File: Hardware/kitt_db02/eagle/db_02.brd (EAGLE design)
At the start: 160 x 100 mm, 30 parts, among them T8.1 TPTP09SQ, T8.2 TPTP09SQ, U8 MCP23017ML, X8.1 CON_HEADER_1X08-SMD

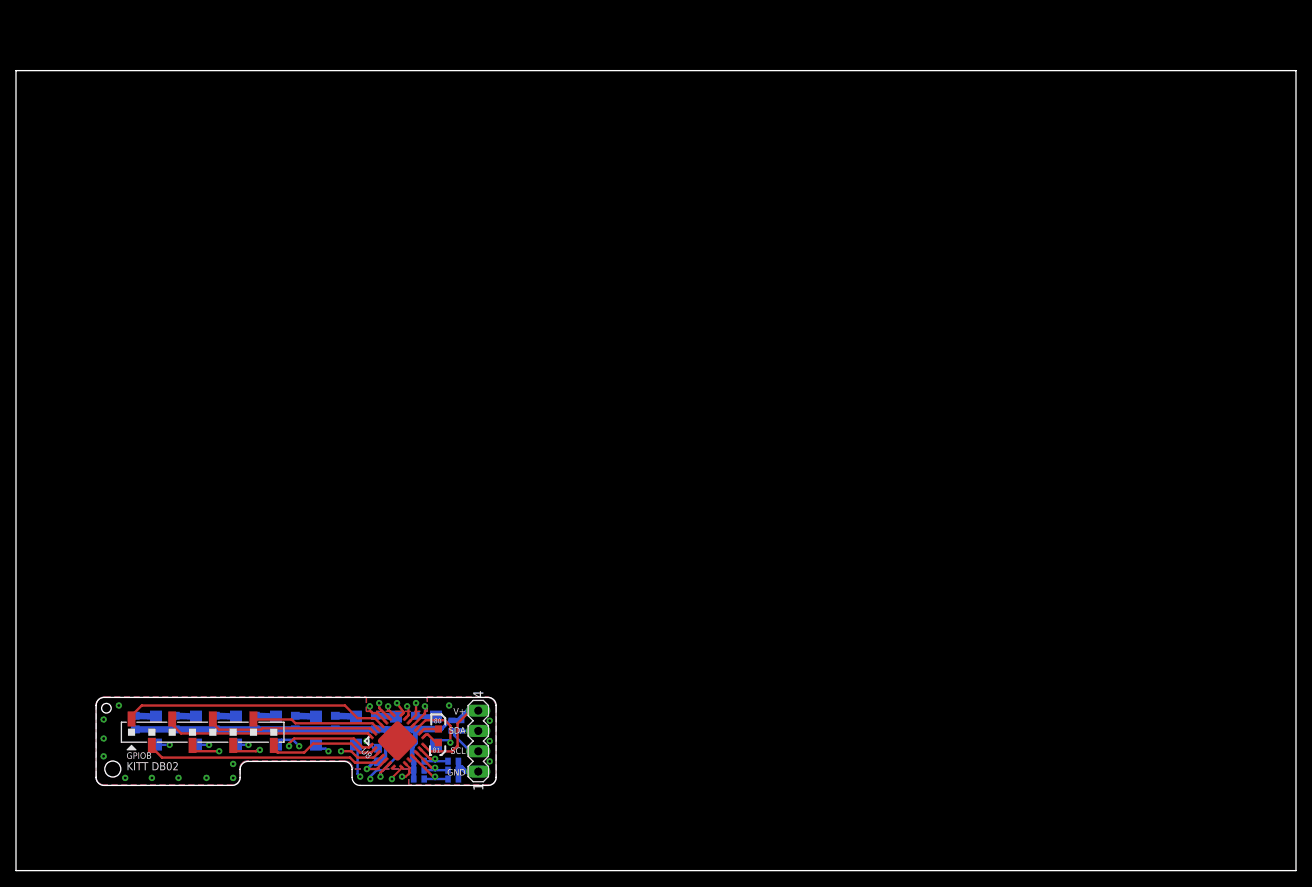
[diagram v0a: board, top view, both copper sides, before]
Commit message: minor touch ups on silkscreen layer
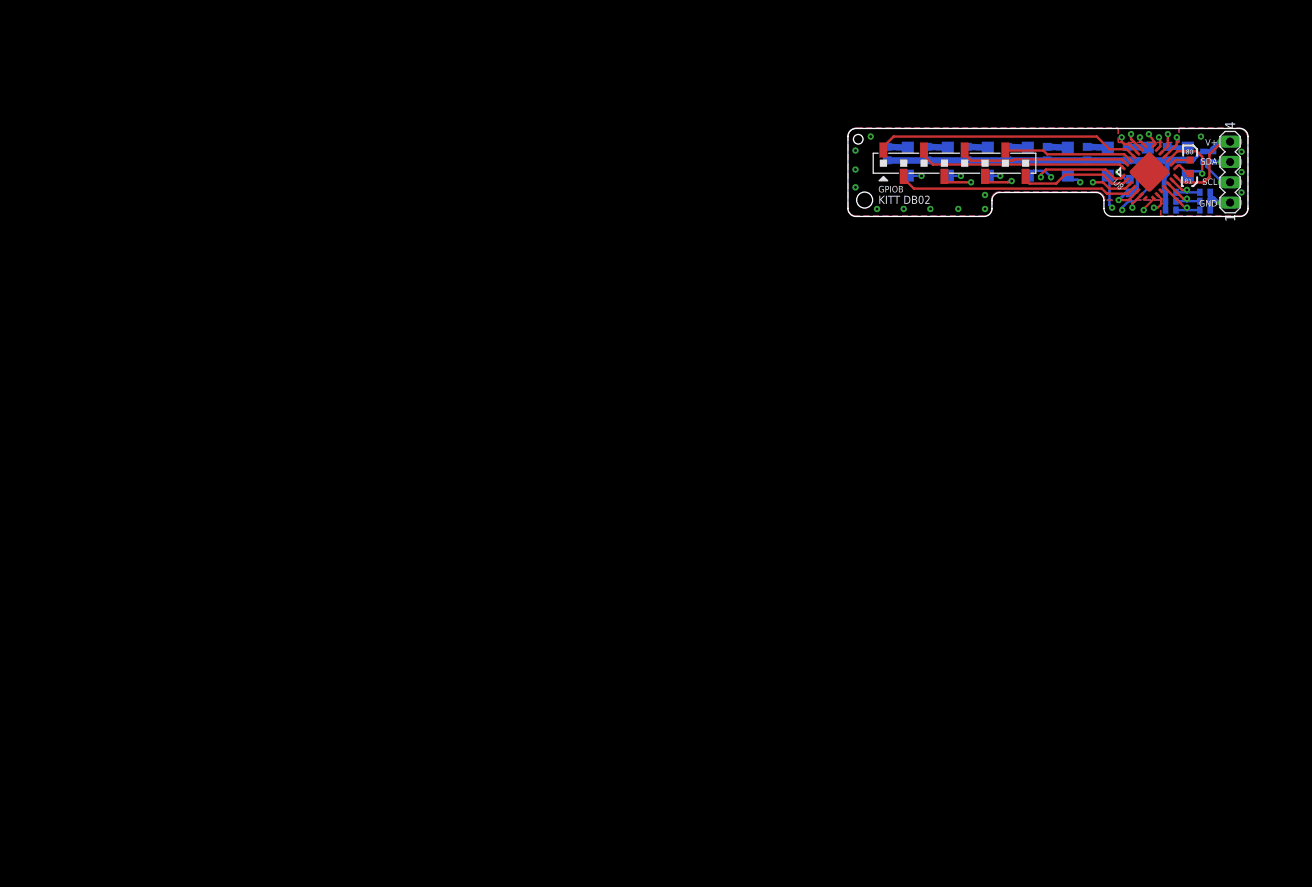
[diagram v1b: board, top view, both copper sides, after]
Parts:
- added U$1: (no value), frames:A4L-LOC
- moved R8.14 117.9 mm to (149.6, 89.2)
- moved C8.0 117.9 mm to (139.2, 85.6)
- moved D8.0 117.9 mm to (146.5, 88.6)
- moved D8.1 117.9 mm to (141.5, 88.6)
- moved D8.2 117.9 mm to (136.5, 88.6)
- moved D8.3 117.9 mm to (131.5, 88.6)
- moved D8.4 117.9 mm to (126.5, 88.6)
- moved D8.5 117.9 mm to (121.5, 88.6)
- moved D8.6 117.9 mm to (116.5, 88.6)
- moved D8.7 117.9 mm to (111.5, 88.6)
- moved R8.0 117.9 mm to (143.9, 89.6)
- moved R8.1 117.9 mm to (138.9, 89.6)
- moved R8.10 117.9 mm to (144.3, 84.8)
- moved R8.13 117.9 mm to (148.6, 84.8)
- moved R8.15 117.9 mm to (148.5, 89.2)
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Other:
- board size 160 x 100 mm -> 50 x 11 mm

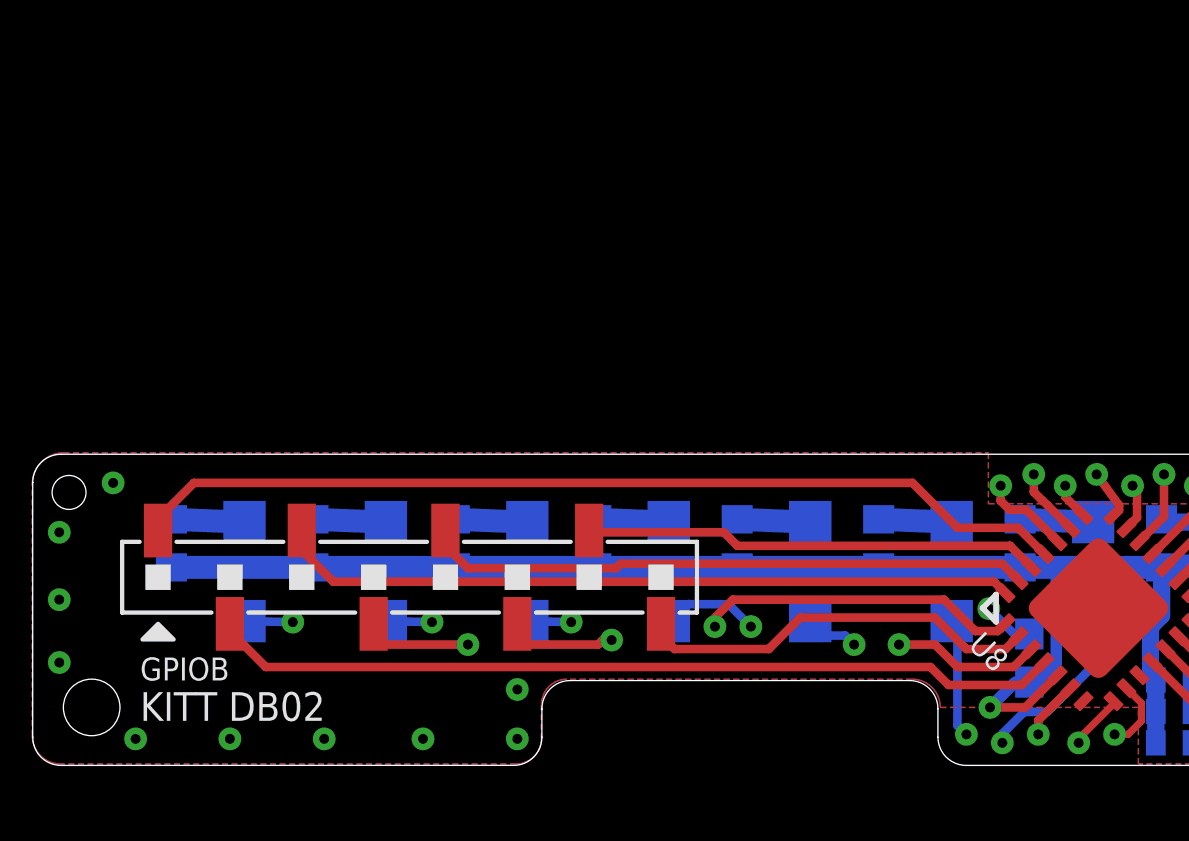
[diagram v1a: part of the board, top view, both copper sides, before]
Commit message: finished bill of materials for db02 -> layout needs a bit more work on the connector,    which now feature gnd and v+
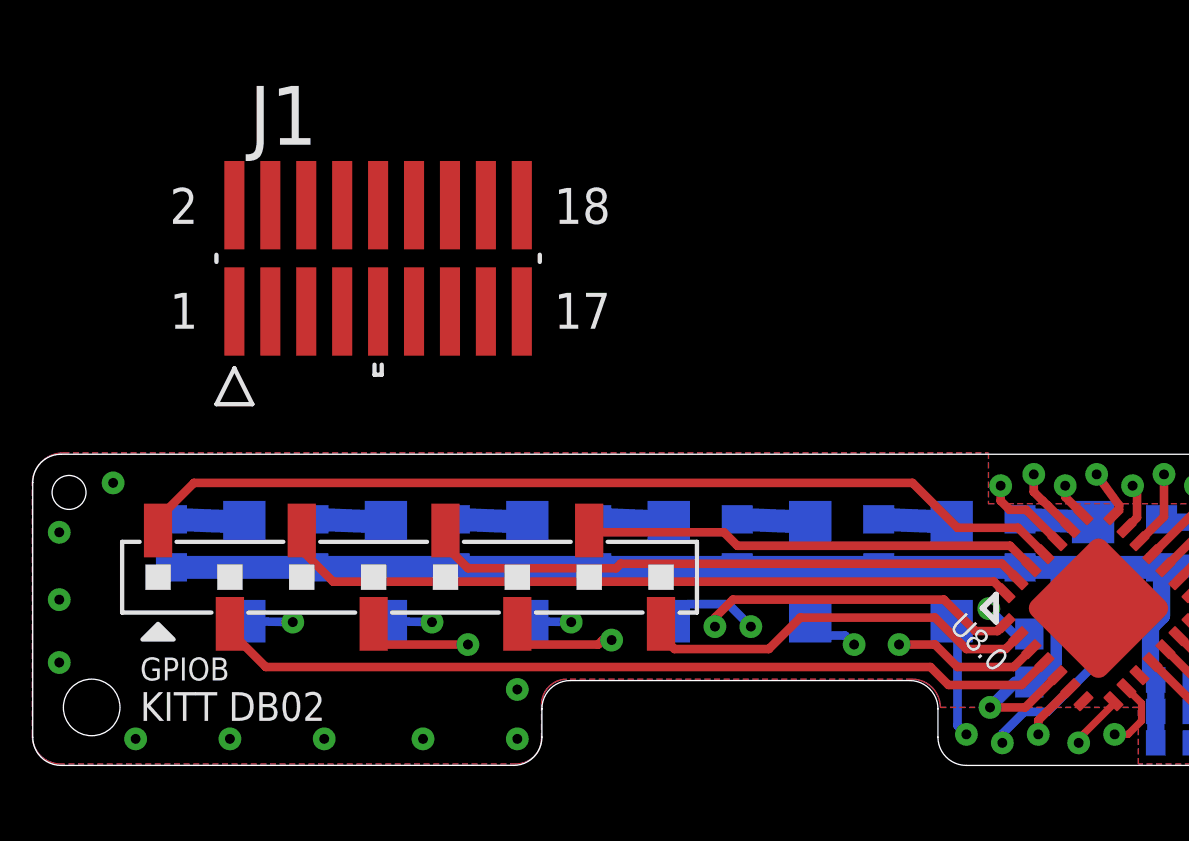
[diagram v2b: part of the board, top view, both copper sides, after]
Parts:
- added J1: FTS-109-01-L-DV, kitt.con:SAMTEC_FTS-109-01-L-DV
- renumbered U8 to U8.0
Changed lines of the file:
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@@
 <attribute name="VALUE" x="114.02" y="89.89" size="1.27" layer="28" rot="MR270"/>
 </element>
-<element name="U8" library="microchip" package="QFN28-ML_6X6MM" value="MCP23017ML" x="141.67" y="87.3275" smashed="yes" rot="R45">
+<element name="U8.0" library="microchip" package="QFN28-ML_6X6MM" value="MCP23017ML" x="141.67" y="87.3275" smashed="yes" rot="R45">
 <attribute name="MF" value="MICROCHIP" x="141.67" y="87.3275" size="1.778" layer="27" rot="R45" display="off"/>
 <attribute name="OC_FARNELL" value="unknown" x="141.67" y="87.3275" size="1.778" layer="27" rot="R45" display="off"/>
@@
 </element>
 <element name="U$1" library="frames" package="A4L-LOC" value="" x="0" y="0"/>
+<element name="J1" library="kitt.con" package="SAMTEC_FTS-109-01-L-DV" value="FTS-109-01-L-DV" x="116.205" y="99.695">
+<attribute name="MF" value="Samtec" x="116.205" y="99.695" size="1.778" layer="27" display="off"/>
+<attribute name="PRICE" value="2.67 USD" x="116.205" y="99.695" size="1.778" layer="27" display="off"/>
+<attribute name="PACKAGE" value="None" x="116.205" y="99.695" size="1.778" layer="27" display="off"/>
+<attribute name="MP" value="FTS-109-01-L-DV" x="116.205" y="99.695" size="1.778" layer="27" display="off"/>
+<attribute name="AVAILABILITY" value="Warning" x="116.205" y="99.695" size="1.778" layer="27" display="off"/>
+<attribute name="DESCRIPTION" value="Conn Unshrouded Header HDR 18 POS 1.27mm Solder ST SMD Tube" x="116.205" y="99.695" size="1.778" layer="27" display="off"/>
+</element>
 </elements>
 <signals>
 <signal name="N$1">
-<contactref element="U8" pad="17"/>
+<contactref element="U8.0" pad="17"/>
 <contactref element="D8.0" pad="C"/>
 <wire x1="148.28" y1="87.12" x2="148.03" y2="87.42" width="0.3048" layer="16"/>
@@
 </signal>
 <signal name="N$2">
-<contactref element="U8" pad="18"/>
+<contactref element="U8.0" pad="18"/>
 <contactref element="D8.1" pad="C"/>
 <wire x1="143.5791875" y1="89.2366875" x2="145.0975" y2="90.755" width="0.3048" layer="1"/>
@@
 </signal>
 <signal name="N$3">
-<contactref element="U8" pad="19"/>
+<contactref element="U8.0" pad="19"/>
 <contactref element="D8.2" pad="C"/>
 <wire x1="143.11956875" y1="89.69630625" x2="143.98625" y2="90.5629875" width="0.3048" layer="1"/>
@@
 </signal>
 <signal name="N$4">
-<contactref element="U8" pad="20"/>
+<contactref element="U8.0" pad="20"/>
 <contactref element="D8.3" pad="C"/>
 <wire x1="142.659946875" y1="90.155925" x2="143.03375" y2="90.529728125" width="0.3048" layer="1"/>
@@
 </signal>
 <signal name="N$5">
-<contactref element="U8" pad="21"/>
+<contactref element="U8.0" pad="21"/>
 <contactref element="D8.4" pad="C"/>
 <wire x1="142.200328125" y1="90.61554375" x2="142.20929375" y2="90.61554375" width="0.3048" layer="1"/>
@@
 </signal>
 <signal name="N$6">
-<contactref element="U8" pad="22"/>
+<contactref element="U8.0" pad="22"/>
 <contactref element="D8.5" pad="C"/>
 <wire x1="141.13966875" y1="90.61554375" x2="140.49375" y2="91.2614625" width="0.3048" layer="1"/>
@@
 </signal>
 <signal name="N$7">
-<contactref element="U8" pad="23"/>
+<contactref element="U8.0" pad="23"/>
 <contactref element="D8.6" pad="C"/>
 <wire x1="140.68005" y1="90.155925" x2="139.872225" y2="90.96375" width="0.3048" layer="1"/>
@@
 </signal>
 <signal name="N$8">
-<contactref element="U8" pad="24"/>
+<contactref element="U8.0" pad="24"/>
 <contactref element="D8.7" pad="C"/>
 <wire x1="140.220428125" y1="89.69630625" x2="139.111734375" y2="90.805" width="0.3048" layer="1"/>
@@
 <wire x1="143.9" y1="88.77" x2="140.17625" y2="88.77" width="0.8128" layer="16"/>
 <contactref element="X8.0" pad="4"/>
-<contactref element="U8" pad="5"/>
+<contactref element="U8.0" pad="5"/>
 <contactref element="R8.14" pad="2"/>
 <contactref element="R8.15" pad="2"/>
@@
 <wire x1="143.51" y1="86.6775" x2="143.9" y2="87.0675" width="0.6096" layer="16"/>
 <wire x1="143.9" y1="87.0675" x2="143.9" y2="88.77" width="0.6096" layer="16"/>
-<contactref element="U8" pad="14"/>
+<contactref element="U8.0" pad="14"/>
 <contactref element="C8.0" pad="1"/>
 <via x="137.83625" y="83.82" extent="1-16" drill="0.35"/>
@@
 <signal name="GND">
 <contactref element="X8.0" pad="1"/>
-<contactref element="U8" pad="6"/>
+<contactref element="U8.0" pad="6"/>
 <wire x1="139.54125" y1="82.8675" x2="139.54125" y2="83.360271875" width="0.3048" layer="1"/>
 <wire x1="139.54125" y1="83.360271875" x2="140.68005" y2="84.499071875" width="0.3048" layer="1"/>
@@
 <contactref element="X8.0" pad="3"/>
 <contactref element="R8.14" pad="1"/>
-<contactref element="U8" pad="8"/>
+<contactref element="U8.0" pad="8"/>
 <wire x1="142.200328125" y1="84.039453125" x2="142.24" y2="83.99978125" width="0.254" layer="1"/>
 <via x="140.97" y="82.5675" extent="1-16" drill="0.35"/>
@@
 <contactref element="X8.0" pad="2"/>
 <contactref element="R8.15" pad="1"/>
-<contactref element="U8" pad="9"/>
+<contactref element="U8.0" pad="9"/>
 <wire x1="142.659946875" y1="84.499071875" x2="143.1925" y2="83.96651875" width="0.254" layer="1"/>
 <wire x1="143.1925" y1="83.96651875" x2="143.1925" y2="83.34375" width="0.254" layer="1"/>
@@
 <contactref element="R8.8" pad="1"/>
 <contactref element="R8.11" pad="2"/>
-<contactref element="U8" pad="11"/>
+<contactref element="U8.0" pad="11"/>
 <wire x1="143.5791875" y1="85.418309375" x2="146.129996875" y2="82.8675" width="0.3048" layer="1"/>
 <wire x1="146.129996875" y1="82.8675" x2="146.3675" y2="82.8675" width="0.3048" layer="1"/>
@@
 <contactref element="R8.9" pad="1"/>
 <contactref element="R8.12" pad="2"/>
-<contactref element="U8" pad="12"/>
+<contactref element="U8.0" pad="12"/>
 <wire x1="144.03880625" y1="85.877928125" x2="145.937984375" y2="83.97875" width="0.3048" layer="1"/>
 <wire x1="145.937984375" y1="83.97875" x2="146.3675" y2="83.97875" width="0.3048" layer="1"/>
@@
 <contactref element="R8.10" pad="1"/>
 <contactref element="R8.13" pad="2"/>
-<contactref element="U8" pad="13"/>
+<contactref element="U8.0" pad="13"/>
 <wire x1="144.498425" y1="86.33755" x2="145.745975" y2="85.09" width="0.3048" layer="1"/>
 <wire x1="145.745975" y1="85.09" x2="146.3675" y2="85.09" width="0.3048" layer="1"/>
@@
 </signal>
 <signal name="GPB0">
-<contactref element="U8" pad="25"/>
+<contactref element="U8.0" pad="25"/>
 <contactref element="X8.1" pad="1"/>
 <wire x1="139.760809375" y1="89.2366875" x2="138.827496875" y2="90.17" width="0.3048" layer="1"/>
@@
 </signal>
 <signal name="GPB1">
-<contactref element="U8" pad="26"/>
+<contactref element="U8.0" pad="26"/>
 <wire x1="139.301190625" y1="88.77706875" x2="138.543259375" y2="89.535" width="0.3048" layer="1"/>
 <wire x1="138.543259375" y1="89.535" x2="128.905" y2="89.535" width="0.3048" layer="1"/>
@@
 <wire x1="119.38" y1="88.74125" x2="118.58625" y2="89.535" width="0.3048" layer="1"/>
 <wire x1="118.58625" y1="89.535" x2="118.58625" y2="90.07375" width="0.3048" layer="1"/>
-<contactref element="U8" pad="27"/>
+<contactref element="U8.0" pad="27"/>
 <wire x1="138.25901875" y1="88.9" x2="138.841571875" y2="88.317446875" width="0.3048" layer="1"/>
 </signal>
 <signal name="GPB3">
 <contactref element="X8.1" pad="3"/>
-<contactref element="U8" pad="28"/>
+<contactref element="U8.0" pad="28"/>
 <wire x1="113.50625" y1="90.07375" x2="113.50625" y2="89.37625" width="0.3048" layer="1"/>
 <wire x1="113.50625" y1="89.37625" x2="114.6175" y2="88.265" width="0.3048" layer="1"/>
@@
 </signal>
 <signal name="GPB4">
-<contactref element="U8" pad="1"/>
+<contactref element="U8.0" pad="1"/>
 <contactref element="X8.1" pad="6"/>
 <wire x1="138.381953125" y1="86.79716875" x2="138.262284375" y2="86.6775" width="0.3048" layer="1"/>
@@
 </signal>
 <signal name="GPB5">
-<contactref element="U8" pad="2"/>
+<contactref element="U8.0" pad="2"/>
 <contactref element="X8.1" pad="8"/>
 <wire x1="138.841571875" y1="86.33755" x2="138.387771875" y2="85.88375" width="0.3048" layer="1"/>
@@
 <wire x1="116.04625" y1="86.0425" x2="116.04625" y2="86.77375" width="0.3048" layer="1"/>
 <wire x1="134.62" y1="86.0425" x2="134.6025" y2="86.0425" width="0.3048" layer="2"/>
-<contactref element="U8" pad="3"/>
+<contactref element="U8.0" pad="3"/>
 <wire x1="138.6720125" y1="85.24875" x2="139.301190625" y2="85.877928125" width="0.3048" layer="1"/>
 <wire x1="119.38" y1="86.0425" x2="120.1025" y2="85.32" width="0.3048" layer="2" curve="90"/>
@@
 <wire x1="112.23625" y1="85.24875" x2="110.96625" y2="86.51875" width="0.3048" layer="1"/>
 <wire x1="110.96625" y1="86.51875" x2="110.96625" y2="86.77375" width="0.3048" layer="1"/>
-<contactref element="U8" pad="4"/>
+<contactref element="U8.0" pad="4"/>
 <wire x1="138.95625" y1="84.61375" x2="139.760809375" y2="85.418309375" width="0.3048" layer="1"/>
 </signal>
 <signal name="N$23">
 <contactref element="T8.1" pad="TP"/>
-<contactref element="U8" pad="16"/>
+<contactref element="U8.0" pad="16"/>
 <wire x1="144.498425" y1="88.317446875" x2="144.498425" y2="88.338425" width="0.3048" layer="1"/>
 <wire x1="144.498425" y1="88.338425" x2="144.98" y2="88.82" width="0.3048" layer="1"/>
@@
 <signal name="N$24">
 <contactref element="T8.2" pad="TP"/>
-<contactref element="U8" pad="15"/>
+<contactref element="U8.0" pad="15"/>
 <wire x1="144.95804375" y1="87.857828125" x2="145.220215625" y2="88.12" width="0.3048" layer="1"/>
 <wire x1="145.220215625" y1="88.12" x2="145.48" y2="88.12" width="0.3048" layer="1"/>
